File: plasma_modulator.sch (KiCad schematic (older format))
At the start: 81 parts, among them P1 CONN_01X03, P2 CONN_01X03, P3 CONN_01X06, P4 CONN_01X04, P5 RCA_1, Q1 MOSFET_N, Q2 MOSFET_N, Q3 MOSFET_N, Q4 MOSFET_N, SW1 SW_PUSH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

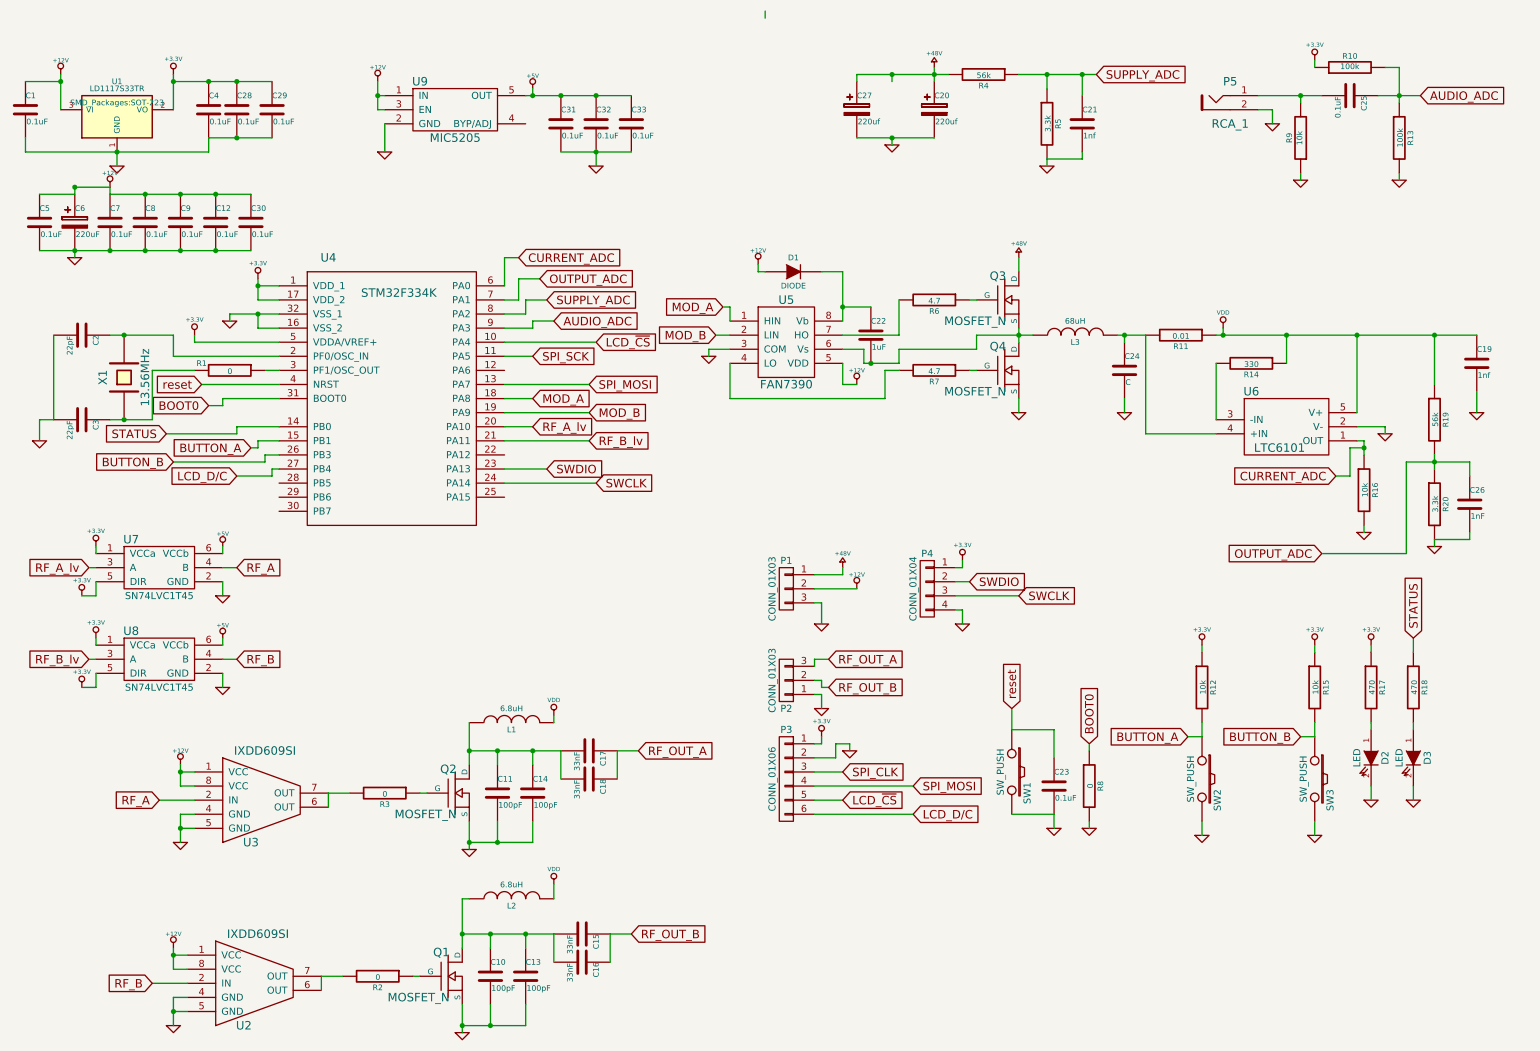
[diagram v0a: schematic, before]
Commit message: draft of component layout
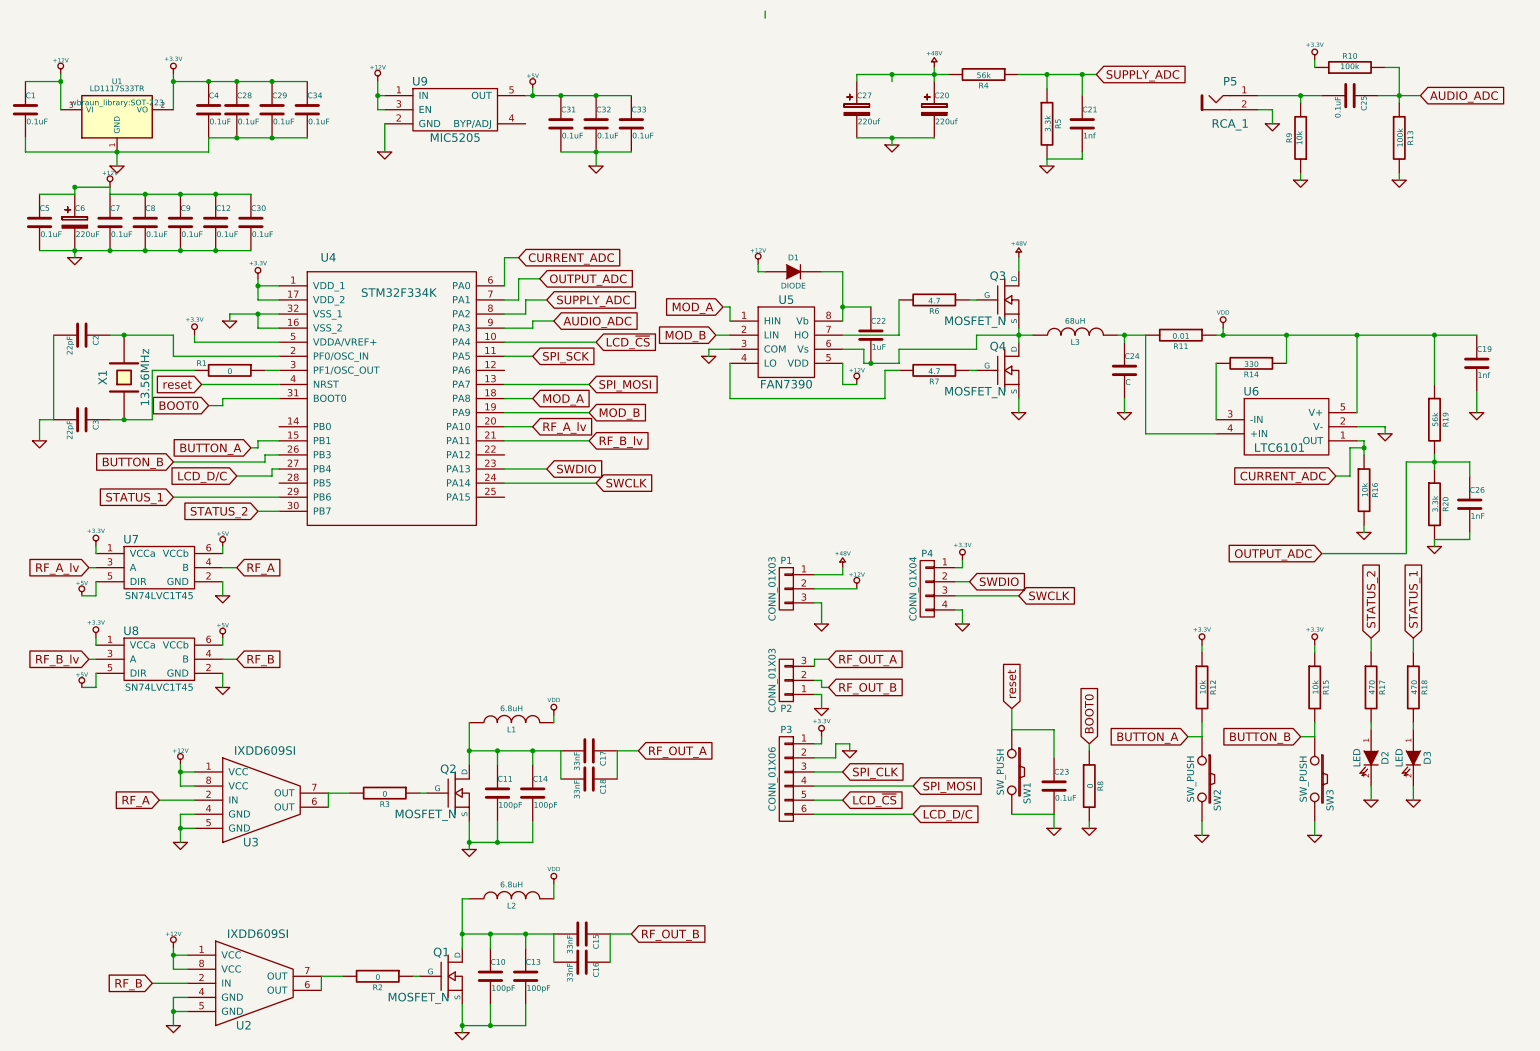
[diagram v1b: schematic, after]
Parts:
- added C34: 0.1uF, wbraun_library:SMD-0805, symbol C
- U1: footprint SMD_Packages:SOT-223 -> wbraun_library:SOT-223
- X1: footprint Crystals:Crystal_HC49-SD_SMD -> wbraun_library:4-SMD
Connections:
- net +3.3V: now also C34.1; no longer R17.1, U7.5 (DIR), U8.5 (DIR)
- net +5V: now also U7.5 (DIR), U8.5 (DIR)
- net GND: now also C34.2
- net STATUS_1: now reaches U4.29 (PB6)
- net STATUS_1: now also R18.1
- net STATUS_2: now reaches U4.30 (PB7)
- net STATUS_2: now also R17.1
- net STATUS: no longer names the net of U4.14 (PB0)
- net STATUS: no longer R18.1
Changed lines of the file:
@@
 F 0 "U1" H 1300 1400 40  0000 C CNN
 F 1 "LD1117S33TR" H 1300 1350 40  0000 C CNN
-F 2 "SMD_Packages:SOT-223" H 1300 1250 40  0000 C CNN
+F 2 "wbraun_library:SOT-223" H 1300 1250 40  0000 C CNN
 F 3 "" H 1300 1150 60  0000 C CNN
 	1    1300 1150
@@
 F 0 "X1" H 1350 3150 60  0000 C CNN
 F 1 "13.56MHz" H 1350 2850 60  0000 C CNN
-F 2 "Crystals:Crystal_HC49-SD_SMD" H 1350 3000 60  0001 C CNN
+F 2 "wbraun_library:4-SMD" H 1350 3000 60  0001 C CNN
 F 3 "" H 1350 3000 60  0000 C CNN
 	1    1350 3000
@@
 	1    0    0    -1
 $EndComp
-$Comp
-L +3.3V #PWR040
-U 1 1 54BB59E0
-P 10200 4900
-F 0 "#PWR040" H 10200 4860 30  0001 C CNN
-F 1 "+3.3V" H 10200 5010 30  0000 C CNN
-F 2 "" H 10200 4900 60  0000 C CNN
-F 3 "" H 10200 4900 60  0000 C CNN
-	1    10200 4900
-	1    0    0    -1
-$EndComp
 Text GLabel 10500 4850 1    60   Input ~ 0
-STATUS
-Text GLabel 1650 3400 0    60   Input ~ 0
-STATUS
+STATUS_1
+Text GLabel 2300 3950 0    60   Input ~ 0
+STATUS_2
 $Comp
 L CONN_01X06 P3
@@
 $EndComp
 $Comp
-L +3.3V #PWR041
+L +3.3V #PWR040
 U 1 1 54BB7915
 P 6300 5550
-F 0 "#PWR041" H 6300 5510 30  0001 C CNN
+F 0 "#PWR040" H 6300 5510 30  0001 C CNN
 F 1 "+3.3V" H 6300 5660 30  0000 C CNN
 F 2 "" H 6300 5550 60  0000 C CNN
@@
 $EndComp
 $Comp
-L GND #PWR042
+L GND #PWR041
 U 1 1 54BB79D7
 P 6500 5650
-F 0 "#PWR042" H 6500 5650 30  0001 C CNN
+F 0 "#PWR041" H 6500 5650 30  0001 C CNN
 F 1 "GND" H 6500 5580 30  0001 C CNN
 F 2 "" H 6500 5650 60  0000 C CNN
@@
 $EndComp
 $Comp
-L +3.3V #PWR043
+L +3.3V #PWR042
 U 1 1 54BBA386
 P 9800 4900
-F 0 "#PWR043" H 9800 4860 30  0001 C CNN
+F 0 "#PWR042" H 9800 4860 30  0001 C CNN
 F 1 "+3.3V" H 9800 5010 30  0000 C CNN
 F 2 "" H 9800 4900 60  0000 C CNN
@@
 $EndComp
 $Comp
-L +3.3V #PWR044
+L +3.3V #PWR043
 U 1 1 54BBA3CF
 P 9000 4900
-F 0 "#PWR044" H 9000 4860 30  0001 C CNN
+F 0 "#PWR043" H 9000 4860 30  0001 C CNN
 F 1 "+3.3V" H 9000 5010 30  0000 C CNN
 F 2 "" H 9000 4900 60  0000 C CNN
@@
 SWCLK
 $Comp
-L GND #PWR045
+L GND #PWR044
 U 1 1 54BBC277
 P 9000 6250
-F 0 "#PWR045" H 9000 6250 30  0001 C CNN
+F 0 "#PWR044" H 9000 6250 30  0001 C CNN
 F 1 "GND" H 9000 6180 30  0001 C CNN
 F 2 "" H 9000 6250 60  0000 C CNN
@@
 $EndComp
 $Comp
-L GND #PWR046
+L GND #PWR045
 U 1 1 54BBC573
 P 9800 6250
-F 0 "#PWR046" H 9800 6250 30  0001 C CNN
+F 0 "#PWR045" H 9800 6250 30  0001 C CNN
 F 1 "GND" H 9800 6180 30  0001 C CNN
 F 2 "" H 9800 6250 60  0000 C CNN
@@
 $EndComp
 $Comp
-L GND #PWR047
+L GND #PWR046
 U 1 1 54BBE80B
 P 7900 1500
-F 0 "#PWR047" H 7900 1500 30  0001 C CNN
+F 0 "#PWR046" H 7900 1500 30  0001 C CNN
 F 1 "GND" H 7900 1430 30  0001 C CNN
 F 2 "" H 7900 1500 60  0000 C CNN
@@
 $EndComp
 $Comp
-L GND #PWR048
+L GND #PWR047
 U 1 1 54BC47B6
 P 9500 1200
-F 0 "#PWR048" H 9500 1200 30  0001 C CNN
+F 0 "#PWR047" H 9500 1200 30  0001 C CNN
 F 1 "GND" H 9500 1130 30  0001 C CNN
 F 2 "" H 9500 1200 60  0000 C CNN
@@
 $EndComp
 $Comp
-L +3.3V #PWR049
+L +3.3V #PWR048
 U 1 1 54BC5953
 P 9800 750
-F 0 "#PWR049" H 9800 710 30  0001 C CNN
+F 0 "#PWR048" H 9800 710 30  0001 C CNN
 F 1 "+3.3V" H 9800 860 30  0000 C CNN
 F 2 "" H 9800 750 60  0000 C CNN
@@
 $EndComp
 $Comp
-L GND #PWR050
+L GND #PWR049
 U 1 1 54BC5B97
 P 9700 1600
-F 0 "#PWR050" H 9700 1600 30  0001 C CNN
+F 0 "#PWR049" H 9700 1600 30  0001 C CNN
 F 1 "GND" H 9700 1530 30  0001 C CNN
 F 2 "" H 9700 1600 60  0000 C CNN
@@
 $EndComp
 $Comp
-L GND #PWR051
+L GND #PWR050
 U 1 1 54BC5C7D
 P 10400 1600
-F 0 "#PWR051" H 10400 1600 30  0001 C CNN
+F 0 "#PWR050" H 10400 1600 30  0001 C CNN
 F 1 "GND" H 10400 1530 30  0001 C CNN
 F 2 "" H 10400 1600 60  0000 C CNN
@@
 $EndComp
 $Comp
-L GND #PWR052
+L GND #PWR051
 U 1 1 54D46650
 P 10950 3250
-F 0 "#PWR052" H 10950 3250 30  0001 C CNN
+F 0 "#PWR051" H 10950 3250 30  0001 C CNN
 F 1 "GND" H 10950 3180 30  0001 C CNN
 F 2 "" H 10950 3250 60  0000 C CNN
@@
 	1700 850  1700 1100
 Wire Wire Line
-	1700 900  2400 900
+	1700 900  2650 900
 Connection ~ 1700 900
 Connection ~ 900  900
@@
 	10500 4850 10500 4950
 Wire Wire Line
-	10200 4900 10200 4950
+	10200 4850 10200 4950
 Wire Wire Line
 	6300 5550 6300 5600
@@
 	2050 3200 1950 3200
 Wire Wire Line
-	1650 3400 2150 3400
-Wire Wire Line
-	2150 3400 2150 3350
-Wire Wire Line
-	2150 3350 2450 3350
-Wire Wire Line
 	2250 3500 2300 3500
 Wire Wire Line
@@
 Connection ~ 2150 900
 Wire Wire Line
-	1950 1300 2400 1300
+	1950 1300 2650 1300
 Connection ~ 2150 1300
 Connection ~ 2000 1700
@@
 $EndComp
 $Comp
-L +12V #PWR053
+L +12V #PWR052
 U 1 1 54D56108
 P 3150 900
-F 0 "#PWR053" H 3150 850 20  0001 C CNN
+F 0 "#PWR052" H 3150 850 20  0001 C CNN
 F 1 "+12V" H 3150 1000 30  0000 C CNN
 F 2 "" H 3150 900 60  0000 C CNN
@@
 	3150 1000 3200 1000
 $Comp
-L +5V #PWR054
+L +5V #PWR053
 U 1 1 54D56583
 P 4250 950
-F 0 "#PWR054" H 4250 1040 20  0001 C CNN
+F 0 "#PWR053" H 4250 1040 20  0001 C CNN
 F 1 "+5V" H 4250 1040 30  0000 C CNN
 F 2 "" H 4250 950 60  0000 C CNN
@@
 $EndComp
 $Comp
-L GND #PWR055
+L GND #PWR054
 U 1 1 54D566F9
 P 4700 1500
-F 0 "#PWR055" H 4700 1500 30  0001 C CNN
+F 0 "#PWR054" H 4700 1500 30  0001 C CNN
 F 1 "GND" H 4700 1430 30  0001 C CNN
 F 2 "" H 4700 1500 60  0000 C CNN
@@
 $EndComp
 $Comp
-L GND #PWR056
+L GND #PWR055
 U 1 1 54D5670D
 P 3200 1400
-F 0 "#PWR056" H 3200 1400 30  0001 C CNN
+F 0 "#PWR055" H 3200 1400 30  0001 C CNN
 F 1 "GND" H 3200 1330 30  0001 C CNN
 F 2 "" H 3200 1400 60  0000 C CNN
@@
 $EndComp
 $Comp
-L +5V #PWR057
+L +5V #PWR056
 U 1 1 54D589DA
 P 2050 4200
-F 0 "#PWR057" H 2050 4290 20  0001 C CNN
+F 0 "#PWR056" H 2050 4290 20  0001 C CNN
 F 1 "+5V" H 2050 4290 30  0000 C CNN
 F 2 "" H 2050 4200 60  0000 C CNN
@@
 $EndComp
 $Comp
-L +5V #PWR058
+L +5V #PWR057
 U 1 1 54D58A90
 P 2050 4850
-F 0 "#PWR058" H 2050 4940 20  0001 C CNN
+F 0 "#PWR057" H 2050 4940 20  0001 C CNN
 F 1 "+5V" H 2050 4940 30  0000 C CNN
 F 2 "" H 2050 4850 60  0000 C CNN
@@
 $EndComp
 $Comp
-L +3.3V #PWR059
+L +3.3V #PWR058
 U 1 1 54D58AF5
 P 1150 4200
-F 0 "#PWR059" H 1150 4160 30  0001 C CNN
+F 0 "#PWR058" H 1150 4160 30  0001 C CNN
 F 1 "+3.3V" H 1150 4310 30  0000 C CNN
 F 2 "" H 1150 4200 60  0000 C CNN
@@
 $EndComp
 $Comp
-L +3.3V #PWR060
+L +3.3V #PWR059
 U 1 1 54D58B09
 P 1150 4850
-F 0 "#PWR060" H 1150 4810 30  0001 C CNN
+F 0 "#PWR059" H 1150 4810 30  0001 C CNN
 F 1 "+3.3V" H 1150 4960 30  0000 C CNN
 F 2 "" H 1150 4850 60  0000 C CNN
@@
 $EndComp
 $Comp
-L +3.3V #PWR061
-U 1 1 54D58B1D
-P 1050 4550
-F 0 "#PWR061" H 1050 4510 30  0001 C CNN
-F 1 "+3.3V" H 1050 4660 30  0000 C CNN
-F 2 "" H 1050 4550 60  0000 C CNN
-F 3 "" H 1050 4550 60  0000 C CNN
-	1    1050 4550
-	1    0    0    -1
-$EndComp
-$Comp
-L +3.3V #PWR062
-U 1 1 54D58B31
-P 1050 5200
-F 0 "#PWR062" H 1050 5160 30  0001 C CNN
-F 1 "+3.3V" H 1050 5310 30  0000 C CNN
-F 2 "" H 1050 5200 60  0000 C CNN
-F 3 "" H 1050 5200 60  0000 C CNN
-	1    1050 5200
-	1    0    0    -1
-$EndComp
-$Comp
-L GND #PWR063
+L GND #PWR060
 U 1 1 54D58B45
 P 2050 4550
-F 0 "#PWR063" H 2050 4550 30  0001 C CNN
+F 0 "#PWR060" H 2050 4550 30  0001 C CNN
 F 1 "GND" H 2050 4480 30  0001 C CNN
 F 2 "" H 2050 4550 60  0000 C CNN
@@
 $EndComp
 $Comp
-L GND #PWR064
+L GND #PWR061
 U 1 1 54D58BB9
 P 2050 5200
-F 0 "#PWR064" H 2050 5200 30  0001 C CNN
+F 0 "#PWR061" H 2050 5200 30  0001 C CNN
 F 1 "GND" H 2050 5130 30  0001 C CNN
 F 2 "" H 2050 5200 60  0000 C CNN
@@
 Wire Wire Line
 	2050 5000 2150 5000
+Wire Wire Line
+	2300 3950 2450 3950
+Text GLabel 1700 3850 0    60   Input ~ 0
+STATUS_1
+Wire Wire Line
+	1700 3850 2450 3850
+Text GLabel 10200 4850 1    60   Input ~ 0
+STATUS_2
+$Comp
+L +5V #PWR062
+U 1 1 54D59595
+P 1050 4550
+F 0 "#PWR062" H 1050 4640 20  0001 C CNN
+F 1 "+5V" H 1050 4640 30  0000 C CNN
+F 2 "" H 1050 4550 60  0000 C CNN
+F 3 "" H 1050 4550 60  0000 C CNN
+	1    1050 4550
+	1    0    0    -1
+$EndComp
+$Comp
+L +5V #PWR063
+U 1 1 54D595A9
+P 1050 5200
+F 0 "#PWR063" H 1050 5290 20  0001 C CNN
+F 1 "+5V" H 1050 5290 30  0000 C CNN
+F 2 "" H 1050 5200 60  0000 C CNN
+F 3 "" H 1050 5200 60  0000 C CNN
+	1    1050 5200
+	1    0    0    -1
+$EndComp
+$Comp
+L C C34
+U 1 1 54D5A879
+P 2650 1100
+F 0 "C34" H 2650 1200 40  0000 L CNN
+F 1 "0.1uF" H 2656 1015 40  0000 L CNN
+F 2 "wbraun_library:SMD-0805" H 2688 950 30  0001 C CNN
+F 3 "" H 2650 1100 60  0000 C CNN
+	1    2650 1100
+	1    0    0    -1
+$EndComp
+Connection ~ 2400 900
+Connection ~ 2400 1300
 $EndSCHEMATC

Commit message: final component placement
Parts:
- removed R8: 0, wbraun_library:SMD-0805, symbol R
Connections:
- net BOOT0 is gone; now on net GND: U4.31 (BOOT0)
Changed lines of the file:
@@
 reset
-$Comp
-L GND #PWR016
-U 1 1 54BB31CD
-P 8200 6200
-F 0 "#PWR016" H 8200 6200 30  0001 C CNN
-F 1 "GND" H 8200 6130 30  0001 C CNN
-F 2 "" H 8200 6200 60  0000 C CNN
-F 3 "" H 8200 6200 60  0000 C CNN
-	1    8200 6200
-	1    0    0    -1
-$EndComp
 $Comp
 L +12V #PWR017
@@
 Text GLabel 4150 2150 2    60   Input ~ 0
 CURRENT_ADC
-$Comp
-L R R8
-U 1 1 54BB305D
-P 8200 5900
-F 0 "R8" V 8280 5900 40  0000 C CNN
-F 1 "0" V 8207 5901 40  0000 C CNN
-F 2 "wbraun_library:SMD-0805" V 8130 5900 30  0001 C CNN
-F 3 "" H 8200 5900 30  0000 C CNN
-	1    8200 5900
-	1    0    0    -1
-$EndComp
-Text GLabel 8200 5600 1    60   Input ~ 0
-BOOT0
-Text GLabel 1950 3200 0    60   Input ~ 0
-BOOT0
 Text GLabel 9950 3700 0    60   Input ~ 0
 CURRENT_ADC
@@
 	2050 3150 2450 3150
 Wire Wire Line
-	8200 5600 8200 5650
-Wire Wire Line
-	8200 6150 8200 6200
-Wire Wire Line
 	6300 2250 6450 2250
 Connection ~ 6450 2500
@@
 	1250 3300 1550 3300
 Wire Wire Line
-	2050 3150 2050 3200
-Wire Wire Line
-	2050 3200 1950 3200
+	2050 3150 2050 3250
 Wire Wire Line
 	2250 3500 2300 3500
@@
 Connection ~ 2400 900
 Connection ~ 2400 1300
+$Comp
+L GND #PWR064
+U 1 1 54D599F9
+P 2050 3250
+F 0 "#PWR064" H 2050 3250 30  0001 C CNN
+F 1 "GND" H 2050 3180 30  0001 C CNN
+F 2 "" H 2050 3250 60  0000 C CNN
+F 3 "" H 2050 3250 60  0000 C CNN
+	1    2050 3250
+	1    0    0    -1
+$EndComp
 $EndSCHEMATC

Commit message: PCB ready for fab
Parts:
- added C35: 3.9nF, wbraun_library:SMD-0805, symbol C
- added C36: 0.1uF, wbraun_library:SMD-0805, symbol C
- added R21: 4.7, wbraun_library:SMD-0805, symbol R
- added R8: 1k, wbraun_library:SMD-0805, symbol R
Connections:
- net SPI_CLK is gone; now on net SPI_SCK: P3.3 (P3)
- net +12V: now also R21.2; no longer D1.1 (A)
- net +3.3V: now also C36.1
- net AUDIO_ADC: now also C35.2, R8.2; no longer C25.1, R10.2, R13.1
- net BUTTON_A: now also U4.27 (PB4); no longer U4.15 (PB1)
- net GND: now also C35.1, C36.2
- net LCD_D/C: now also U4.14 (PB0); no longer U4.27 (PB4)
- net RF_OUT_A: now also P2.2 (P2); no longer P2.3 (P3)
- net RF_OUT_B: now also P2.3 (P3); no longer P2.2 (P2)
- new net: D1.1 (A), R21.1
- new net: C25.1, R10.2, R13.1, R8.1
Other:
- moved on the sheet: C25, P5, R10, R13, R9
